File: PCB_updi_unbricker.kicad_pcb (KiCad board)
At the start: 2 copper layers, 54 x 47.5 mm, 63 parts, among them J1 USB_C_Receptacle_USB2.0_16P, J2 Target, J3 TTL Serial, J4 RTS / DTR, J5 UPDI_TINY, J6 UPDI_DxEx, J7 UPDI_FW, Q3 BSS138, Q4 AO3401A, Q5 BSS84, Q6 BSS138, Q7 BSS84, Q8 BSS138, SW1 HV, SW2 VDD, SW3 Power, SW4 START, U1 CH340K, U2 LM1117GS-3.3, U3 74LVC1G3157, U4 ATtiny412-SS, U5 TPS61040DBV

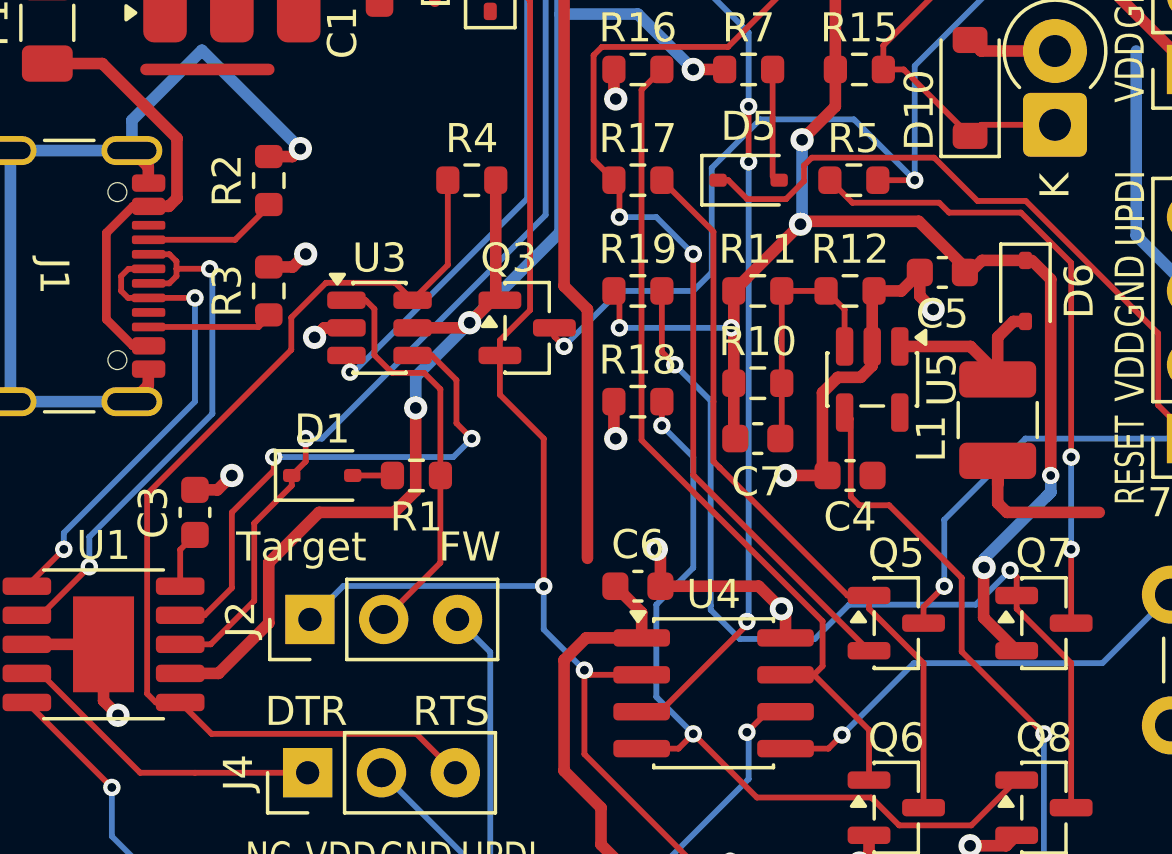
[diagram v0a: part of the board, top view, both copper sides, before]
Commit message: Update
* Change C6 size.
* Use +5V for 74LVC1G3157.
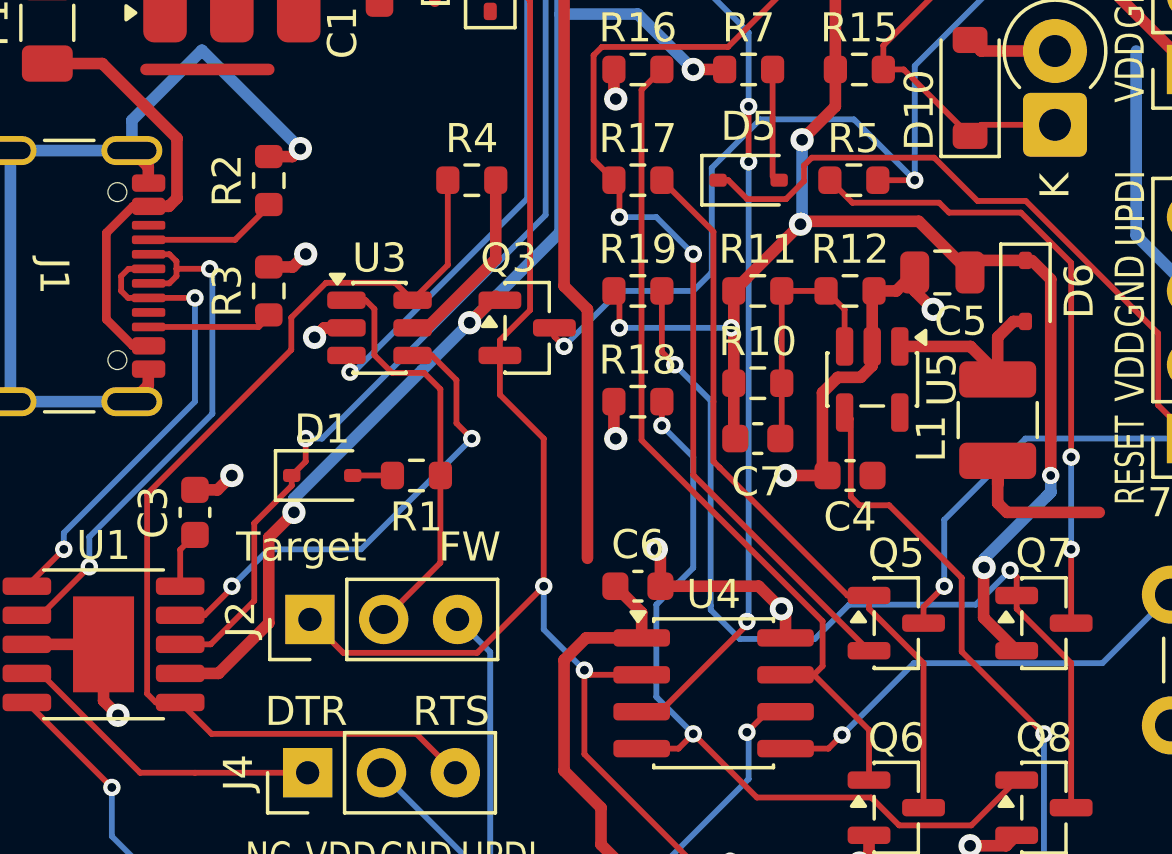
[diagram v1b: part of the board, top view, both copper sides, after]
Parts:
- C5: footprint Capacitor_SMD:C_0603_1608Metric -> Capacitor_SMD:C_0805_2012Metric
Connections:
- R4 pad 2: VDD -> +5V
- U3 pad 5: VDD -> +5V
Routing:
- net VDD: track 68.0 -> 60.5 mm
- net +5V: track 55.9 -> 62.4 mm
- net RxD: track 18.4 -> 16.7 mm
- net UPDI_TGT: track 98.2 -> 99.2 mm

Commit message: Revise routing
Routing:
- net +12V: track 50.9 -> 52.4 mm
- net HV_12: track 21.9 -> 23.2 mm
- net HV_75: track 36.4 -> 35.3 mm
- net HV_12_CTL: track 28.0 -> 26.9 mm
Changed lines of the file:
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@@
 	)
 	(segment
+		(start 112.33 67.465)
+		(end 109.855 64.99)
+		(width 0.4)
+		(layer "F.Cu")
+		(net "+12V")
+	)
+	(segment
 		(start 99.82 71.109)
 		(end 99.809 71.12)
@@
 	)
 	(segment
+		(start 112.33 67.465)
+		(end 112.33 72.391398)
+		(width 0.4)
+		(layer "F.Cu")
+		(net "+12V")
+	)
+	(segment
 		(start 99.82 69.215)
 		(end 99.82 67.31)
@@
 	)
 	(segment
-		(start 110.725 65.64)
-		(end 110.075 64.99)
-		(width 0.4)
-		(layer "F.Cu")
-		(net "+12V")
-	)
-	(segment
-		(start 110.725 65.64)
-		(end 110.725 72.39)
-		(width 0.4)
-		(layer "F.Cu")
-		(net "+12V")
-	)
-	(segment
 		(start 102.215 63.645)
 		(end 106.185 63.645)
@@
 	)
 	(segment
-		(start 110.075 64.99)
-		(end 109.855 64.99)
-		(width 0.2)
-		(layer "F.Cu")
-		(net "+12V")
-	)
-	(segment
 		(start 108.431662 75.648338)
 		(end 108.431662 75.555924)
@@
 	)
 	(via
-		(at 110.725 72.39)
-		(size 0.6)
-		(drill 0.3)
+		(at 112.33 72.391398)
+		(size 0.8)
+		(drill 0.4)
 		(layers "F.Cu" "B.Cu")
 		(net "+12V")
@@
 	)
 	(segment
-		(start 110.57753 73.11253)
-		(end 110.7275 72.96256)
-		(width 0.4)
-		(layer "B.Cu")
-		(net "+12V")
-	)
-	(segment
 		(start 102.169685 60.83891)
 		(end 102.169685 63.690315)
@@
 	)
 	(segment
-		(start 108.431662 75.258398)
-		(end 110.57753 73.11253)
-		(width 0.4)
-		(layer "B.Cu")
-		(net "+12V")
-	)
-	(segment
-		(start 110.57753 73.11253)
-		(end 110.725 72.96506)
+		(start 109.692586 74.295)
+		(end 108.431662 75.555924)
 		(width 0.4)
 		(layer "B.Cu")
@@
 	)
 	(segment
-		(start 108.431662 75.555924)
-		(end 108.431662 75.258398)
+		(start 112.395 72.39)
+		(end 110.49 74.295)
 		(width 0.4)
 		(layer "B.Cu")
@@
 	)
 	(segment
-		(start 110.725 72.96506)
-		(end 110.725 72.39)
+		(start 110.49 74.295)
+		(end 109.692586 74.295)
 		(width 0.4)
 		(layer "B.Cu")
@@
 	)
 	(segment
-		(start 107.227106 63.345)
-		(end 106.887106 63.005)
+		(start 106.887106 63.005)
+		(end 103.9 63.005)
 		(width 0.2)
 		(layer "F.Cu")
@@
 	)
 	(segment
-		(start 109.7 63.345)
-		(end 107.227106 63.345)
+		(start 113.03 66.675)
+		(end 109.7 63.345)
 		(width 0.2)
 		(layer "F.Cu")
@@
 	)
 	(segment
-		(start 106.887106 63.005)
-		(end 103.9 63.005)
+		(start 103.9 63.005)
+		(end 103.125 62.23)
 		(width 0.2)
 		(layer "F.Cu")
@@
 	)
 	(segment
-		(start 103.9 63.005)
-		(end 103.125 62.23)
+		(start 113.03 71.755)
+		(end 113.03 66.675)
 		(width 0.2)
 		(layer "F.Cu")
@@
 	)
 	(segment
-		(start 111.4275 71.755)
-		(end 111.4275 65.0725)
+		(start 107.227106 63.345)
+		(end 106.887106 63.005)
 		(width 0.2)
 		(layer "F.Cu")
@@
 	)
 	(segment
-		(start 111.4275 65.0725)
-		(end 109.7 63.345)
+		(start 109.7 63.345)
+		(end 107.227106 63.345)
 		(width 0.2)
 		(layer "F.Cu")
@@
 	)
 	(via
-		(at 111.4275 71.755)
+		(at 113.03 71.755)
 		(size 0.6)
 		(drill 0.3)
@@
 	)
 	(segment
-		(start 111.4275 71.755)
-		(end 111.4275 74.93)
+		(start 111.4275 74.93)
+		(end 113.03 73.3275)
+		(width 0.2)
+		(layer "B.Cu")
+		(net "HV_12")
+	)
+	(segment
+		(start 113.03 73.3275)
+		(end 113.03 71.755)
 		(width 0.2)
 		(layer "B.Cu")
@@
 	)
 	(segment
-		(start 88.7675 68.26)
-		(end 89.429999 68.26)
+		(start 90.805 69.85)
+		(end 90.805 71.12)
 		(width 0.2)
 		(layer "F.Cu")
@@
 	)
 	(segment
-		(start 90.2775 70.5925)
-		(end 90.805 71.12)
-		(width 0.2)
-		(layer "F.Cu")
-		(net "RxD")
-	)
-	(segment
-		(start 90.2775 69.1075)
-		(end 90.2775 70.5925)
+		(start 88.7675 68.26)
+		(end 89.215 68.26)
 		(width 0.2)
 		(layer "F.Cu")
@@
 	)
 	(segment
-		(start 89.429999 68.26)
-		(end 90.2775 69.1075)
+		(start 89.215 68.26)
+		(end 90.805 69.85)
 		(width 0.2)
 		(layer "F.Cu")
@@
 	)
 	(segment
+		(start 99.06 86.36)
+		(end 100.33 86.36)
+		(width 0.2)
+		(layer "F.Cu")
+		(net "UPDI_TGT")
+	)
+	(segment
 		(start 86.384992 78.493)
 		(end 90.987 78.493)
@@
 	)
 	(segment
+		(start 98.36 85.66)
+		(end 99.06 86.36)
+		(width 0.2)
+		(layer "F.Cu")
+		(net "UPDI_TGT")
+	)
+	(segment
 		(start 94.839472 79.248)
 		(end 94.68 79.088528)
@@
 	)
 	(segment
-		(start 92.81 66.700552)
-		(end 91.7725 67.738052)
+		(start 100.33 86.36)
+		(end 100.3625 86.3275)
 		(width 0.2)
 		(layer "F.Cu")
@@
 	)
 	(segment
-		(start 94.68 81.98)
-		(end 98.36 85.66)
+		(start 92.81 66.700552)
+		(end 91.7725 67.738052)
 		(width 0.2)
 		(layer "F.Cu")
@@
 	)
 	(segment
-		(start 98.36 85.66)
-		(end 99.695 85.66)
+		(start 94.68 81.98)
+		(end 98.36 85.66)
 		(width 0.2)
 		(layer "F.Cu")
@@
 	)
 	(via
-		(at 94.68 79.088528)
+		(at 100.3625 86.3275)
 		(size 0.6)
 		(drill 0.3)
@@
 	)
 	(via
-		(at 93.28 76.2)
+		(at 94.68 79.088528)
 		(size 0.6)
 		(drill 0.3)
@@
 	)
 	(via
-		(at 99.695 85.66)
+		(at 93.28 76.2)
 		(size 0.6)
 		(drill 0.3)
@@
 	(segment
 		(start 102.815 88.78)
-		(end 99.695 85.66)
+		(end 100.3625 86.3275)
 		(width 0.2)
 		(layer "B.Cu")
@@
 	)
 	(segment
-		(start 97.155 76.835)
-		(end 98.425 75.565)
-		(width 0.2)
-		(layer "B.Cu")
-		(net "HV_12_CTL")
-	)
-	(segment
 		(start 98.425 71.755)
-		(end 97.345 70.675)
+		(end 98.425 81.28)
 		(width 0.2)
 		(layer "B.Cu")
@@
 	)
 	(segment
-		(start 98.425 75.565)
+		(start 97.345 70.675)
 		(end 98.425 71.755)
 		(width 0.2)
@@
 	)
 	(segment
-		(start 98.425 81.28)
-		(end 97.155 80.01)
-		(width 0.2)
-		(layer "B.Cu")
-		(net "HV_12_CTL")
-	)
-	(segment
-		(start 97.155 80.01)
-		(end 97.155 76.835)
-		(width 0.2)
-		(layer "B.Cu")
-		(net "HV_12_CTL")
-	)
-	(segment
 		(start 97.345 68.135)
 		(end 97.79 68.58)
@@
 	)
 	(segment
-		(start 109.855 71.12)
-		(end 107.061 73.914)
+		(start 109.855 73.66)
+		(end 112.395 71.12)
 		(width 0.2)
 		(layer "B.Cu")
@@
 	)
 	(segment
-		(start 115.57 71.12)
-		(end 109.855 71.12)
+		(start 109.22 73.66)
+		(end 109.855 73.66)
 		(width 0.2)
 		(layer "B.Cu")
@@
 	)
 	(segment
-		(start 107.061 73.914)
-		(end 107.061 76.2)
+		(start 107.061 75.819)
+		(end 109.22 73.66)
+		(width 0.2)
+		(layer "B.Cu")
+		(net "HV_75")
+	)
+	(segment
+		(start 107.061 76.2)
+		(end 107.061 75.819)
+		(width 0.2)
+		(layer "B.Cu")
+		(net "HV_75")
+	)
+	(segment
+		(start 115.57 71.12)
+		(end 112.395 71.12)
 		(width 0.2)
 		(layer "B.Cu")

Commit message: Revise routing
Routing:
- net HV_75: track 35.3 -> 36.4 mm
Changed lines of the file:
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@@
 	)
 	(segment
-		(start 106.3475 77.47)
-		(end 106.3475 76.9135)
+		(start 106.68 77.8025)
+		(end 106.3475 77.47)
 		(width 0.2)
 		(layer "F.Cu")
@@
 		(start 114.42 69.97)
 		(end 114.42 67.499314)
-		(width 0.2)
-		(layer "F.Cu")
-		(net "HV_75")
-	)
-	(segment
-		(start 106.3475 76.9135)
-		(end 107.061 76.2)
 		(width 0.2)
 		(layer "F.Cu")
@@
 	)
 	(segment
+		(start 106.68 78.105)
+		(end 106.68 77.8025)
+		(width 0.2)
+		(layer "F.Cu")
+		(net "HV_75")
+	)
+	(segment
 		(start 102.235 62.26148)
 		(end 101.61648 62.88)
@@
 	)
 	(via
-		(at 107.061 76.2)
+		(at 106.68 78.105)
 		(size 0.6)
 		(drill 0.3)
@@
 	)
 	(segment
-		(start 109.855 73.66)
-		(end 112.395 71.12)
-		(width 0.2)
-		(layer "B.Cu")
-		(net "HV_75")
-	)
-	(segment
-		(start 109.22 73.66)
-		(end 109.855 73.66)
-		(width 0.2)
-		(layer "B.Cu")
-		(net "HV_75")
-	)
-	(segment
-		(start 107.061 75.819)
-		(end 109.22 73.66)
-		(width 0.2)
-		(layer "B.Cu")
-		(net "HV_75")
-	)
-	(segment
-		(start 107.061 76.2)
-		(end 107.061 75.819)
+		(start 109.855 78.105)
+		(end 106.68 78.105)
 		(width 0.2)
 		(layer "B.Cu")
@@
 	(segment
 		(start 115.57 71.12)
-		(end 112.395 71.12)
+		(end 115.57 72.39)
 		(width 0.2)
 		(layer "B.Cu")
+		(net "HV_75")
+	)
+	(segment
+		(start 115.57 72.39)
+		(end 109.855 78.105)
+		(width 0.2)
+		(layer "B.Cu")
+		(net "HV_75")
+	)
+	(segment
+		(start 106.8225 78.2475)
+		(end 106.68 78.105)
+		(width 0.2)
+		(layer "B.Cu")
